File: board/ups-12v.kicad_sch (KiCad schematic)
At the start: 44 parts, among them J1 USB_B, J11 Front Panel, J12 Battery Meter, J13 TEMP, J14 V_in, J2 Balancig, J7 BAT, J8 Mini Buck Module, Q2 AOD423, SW2 SW_SPDT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

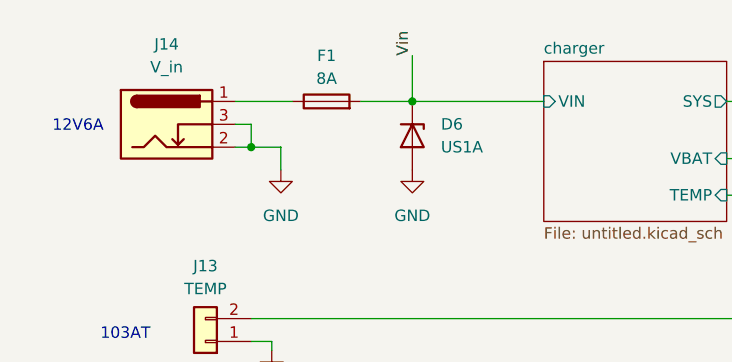
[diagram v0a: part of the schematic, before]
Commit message: incorporate review feedback
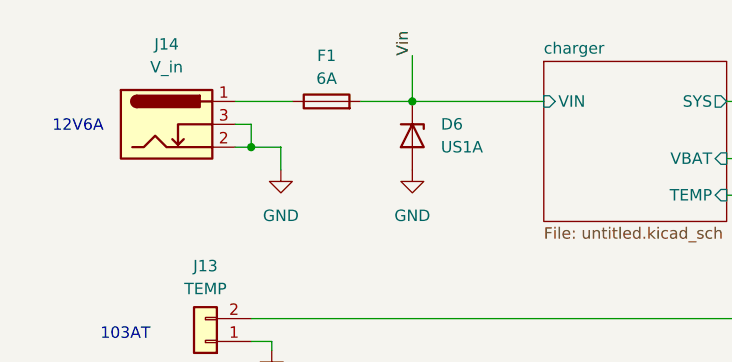
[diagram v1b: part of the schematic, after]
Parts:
- F1: value 8A -> 6A
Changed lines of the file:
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@@
       (effects (font (size 1.27 1.27)))
     )
-    (property "Value" "8A" (at 58.928 36.83 90)
+    (property "Value" "6A" (at 58.928 36.83 90)
       (effects (font (size 1.27 1.27)))
     )
